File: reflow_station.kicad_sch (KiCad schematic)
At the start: 260 parts, among them IC1 AMC23C10DWVR, IC2 MP100LGN-Z, J1 1731734, J10 DG301-5.0-02P-12-00A_H_, J11 USB_A, J12 USB_C_Receptacle_USB2.0_16P, J13 Conn_ARM_JTAG_SWD_10, J2 1707027, J3 1707027, J4 F52Q-1A7H1-11015, J5 1707027, J6 1707027, J7 DG301-5.0-02P-12-00A_H_, J8 DG301-5.0-02P-12-00A_H_, J9 DG301-5.0-02P-12-00A_H_, M1 Fan_CPU_4pin, M2 Fan_CPU_4pin, M3 Fan_CPU_4pin, M4 Fan_CPU_4pin, P1 IEC_60320_C13_Plug, Q1 BTA16-600B, Q2 BTA16-600B, Q3 BTA16-600B, Q4 BTA16-600B, Q5 KSC1815YTA, SW1 SW_DPST_x2, SW2 SW_DIP_x08, SW3 SW_SPST, SW4 SW_SPST, SW5 SW_SPST, SW6 SW_Push, SW7 SW_SPDT, SW8 SW_SPDT, U1 TPS82130, U10 TPS2051BDBVR, U11 RCLAMP0504F.TCT, U12 STM32F469VITx, U13 RCLAMP0504F.TCT, U14 RCLAMP0504F.TCT, U2 RAC20-12SK, U3 MOC3023M, U4 MOC3023M, U5 TPS82130, U6 MOC3023M, U7 MOC3023M, U8 ADS1118IDGS, U9 ADS1118IDGS, Y1 25MHz, Y2 32.768kHz

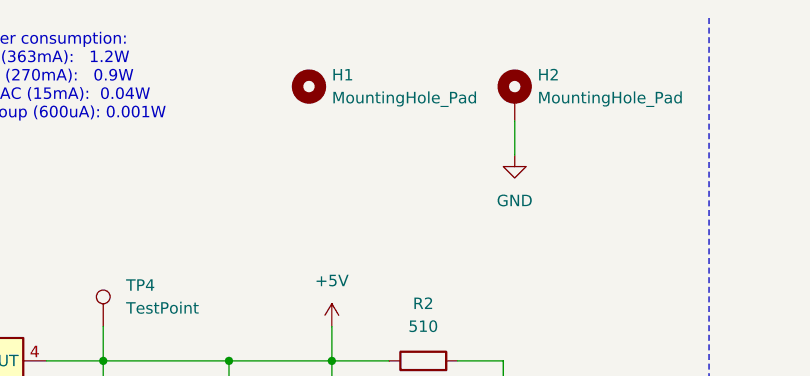
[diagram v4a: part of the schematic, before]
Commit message: feat: update library; change 2P connector for heaters
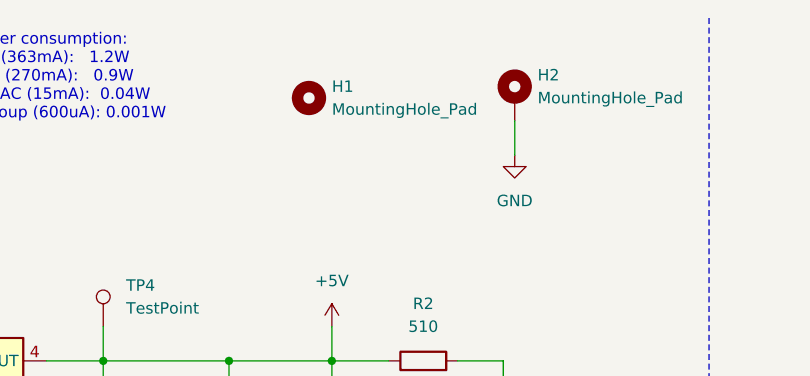
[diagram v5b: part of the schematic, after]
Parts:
- H1: symbol Mechanical:MountingHole -> reflow_station_symbols:MountingHole
- H2, H3, H4: symbol Mechanical:MountingHole_Pad -> reflow_station_symbols:MountingHole_Pad
- J2, J3, J5, J6: footprint reflow_station_library:1707027 -> 1731721; symbol reflow_station_symbols:1707027 -> reflow_station_symbols:1731721; Height 10 -> 18.2; Manufacturer_Part_Number 1707027 -> 1731721
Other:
- moved on the sheet: H1
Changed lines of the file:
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@@
 	)
 	(symbol
-		(lib_id "reflow_station_symbols:1707027")
+		(lib_id "reflow_station_symbols:1731721")
 		(at 1007.11 104.14 90)
 		(mirror x)
@@
 			)
 		)
-		(property "Footprint" "reflow_station_library:1707027"
+		(property "Footprint" "1731721"
 			(at 1102.03 120.65 0)
 			(hide yes)
@@
 			)
 		)
-		(property "Datasheet" "https://www.phoenixcontact.com/en-us/products/printed-circuit-board-terminal-gmkdsn-15-2-762-1707027?type=pdf"
+		(property "Datasheet" "https://www.phoenixcontact.com/en-us/products/printed-circuit-board-terminal-gmkds-3-2-762-1731721?type=pdf"
 			(at 1202.03 120.65 0)
 			(hide yes)
@@
 			)
 		)
-		(property "Description" "GMKDSN 1,5/ 2-7,62 - Printed circuit board terminal, nominal current: 16 A, rated voltage (III/2): 630 V, nominal cross section: 1.5 mm<sup>2</sup>, number of potentials: 2, number of rows: 1, number of positions per row: 2, product range: GMKDSN 1,5, pitch: 7.62 mm, connection method: Screw connection with tension sleeve, screw head form: L Slotted, mounting: Wave soldering, conductor/PCB connection direction: 0 , color: green, Pin layout: Linear pinning, Solder pin [P]: 3.5 mm, number of solder pins per"
+		(property "Description" "GMKDS 3/ 2-7,62 - Printed circuit board terminal, nominal current: 24 A, rated voltage (III/2): 630 V, nominal cross section: 2.5 mm<sup>2</sup>, number of potentials: 2, number of rows: 1, number of positions per row: 2, product range: GMKDS 3, pitch: 7.62 mm, connection method: Screw connection with tension sleeve, screw head form: L Slotted, mounting: Wave soldering, conductor/PCB connection direction: 0 , color: green, Pin layout: Linear pinning, Solder pin [P]: 5 mm, number of solder pins per potentia"
 			(at 1007.11 104.14 0)
 			(hide yes)
@@
 			)
 		)
-		(property "Height" "10"
+		(property "Height" "18.2"
 			(at 1402.03 120.65 0)
 			(hide yes)
@@
 			)
 		)
-		(property "Manufacturer_Part_Number" "1707027"
+		(property "Manufacturer_Part_Number" "1731721"
 			(at 1802.03 120.65 0)
 			(hide yes)
@@
 	)
 	(symbol
-		(lib_id "Mechanical:MountingHole_Pad")
+		(lib_id "reflow_station_symbols:MountingHole_Pad")
 		(at 63.5 515.62 0)
 		(unit 1)
@@
 	)
 	(symbol
-		(lib_id "reflow_station_symbols:1707027")
+		(lib_id "reflow_station_symbols:1731721")
 		(at 1158.24 218.44 90)
 		(mirror x)
@@
 			)
 		)
-		(property "Footprint" "reflow_station_library:1707027"
+		(property "Footprint" "1731721"
 			(at 1253.16 234.95 0)
 			(hide yes)
@@
 			)
 		)
-		(property "Datasheet" "https://www.phoenixcontact.com/en-us/products/printed-circuit-board-terminal-gmkdsn-15-2-762-1707027?type=pdf"
+		(property "Datasheet" "https://www.phoenixcontact.com/en-us/products/printed-circuit-board-terminal-gmkds-3-2-762-1731721?type=pdf"
 			(at 1353.16 234.95 0)
 			(hide yes)
@@
 			)
 		)
-		(property "Description" "GMKDSN 1,5/ 2-7,62 - Printed circuit board terminal, nominal current: 16 A, rated voltage (III/2): 630 V, nominal cross section: 1.5 mm<sup>2</sup>, number of potentials: 2, number of rows: 1, number of positions per row: 2, product range: GMKDSN 1,5, pitch: 7.62 mm, connection method: Screw connection with tension sleeve, screw head form: L Slotted, mounting: Wave soldering, conductor/PCB connection direction: 0 , color: green, Pin layout: Linear pinning, Solder pin [P]: 3.5 mm, number of solder pins per"
+		(property "Description" "GMKDS 3/ 2-7,62 - Printed circuit board terminal, nominal current: 24 A, rated voltage (III/2): 630 V, nominal cross section: 2.5 mm<sup>2</sup>, number of potentials: 2, number of rows: 1, number of positions per row: 2, product range: GMKDS 3, pitch: 7.62 mm, connection method: Screw connection with tension sleeve, screw head form: L Slotted, mounting: Wave soldering, conductor/PCB connection direction: 0 , color: green, Pin layout: Linear pinning, Solder pin [P]: 5 mm, number of solder pins per potentia"
 			(at 1158.24 218.44 0)
 			(hide yes)
@@
 			)
 		)
-		(property "Height" "10"
+		(property "Height" "18.2"
 			(at 1553.16 234.95 0)
 			(hide yes)
@@
 			)
 		)
-		(property "Manufacturer_Part_Number" "1707027"
+		(property "Manufacturer_Part_Number" "1731721"
 			(at 1953.16 234.95 0)
 			(hide yes)
@@
 	)
 	(symbol
-		(lib_id "Mechanical:MountingHole")
-		(at 316.23 20.32 0)
+		(lib_id "reflow_station_symbols:MountingHole")
+		(at 316.23 21.59 0)
 		(unit 1)
 		(body_style 1)
@@
 		(fields_autoplaced yes)
 		(property "Reference" "H1"
-			(at 318.77 19.0499 0)
+			(at 318.77 20.3199 0)
 			(show_name no)
 			(do_not_autoplace no)
@@
 		)
 		(property "Value" "MountingHole_Pad"
-			(at 318.77 21.5899 0)
+			(at 318.77 22.8599 0)
 			(show_name no)
 			(do_not_autoplace no)
@@
 		)
 		(property "Footprint" "MountingHole:MountingHole_3mm"
-			(at 316.23 20.32 0)
+			(at 316.23 21.59 0)
 			(hide yes)
 			(show_name no)
@@
 		)
 		(property "Datasheet" ""
-			(at 316.23 20.32 0)
+			(at 316.23 21.59 0)
 			(hide yes)
 			(show_name no)
@@
 		)
 		(property "Description" "Mounting Hole without connection"
-			(at 316.23 20.32 0)
+			(at 316.23 21.59 0)
 			(hide yes)
 			(show_name no)
@@
 	)
 	(symbol
-		(lib_id "reflow_station_symbols:1707027")
+		(lib_id "reflow_station_symbols:1731721")
 		(at 1007.11 218.44 90)
 		(mirror x)
@@
 			)
 		)
-		(property "Footprint" "reflow_station_library:1707027"
+		(property "Footprint" "1731721"
 			(at 1102.03 234.95 0)
 			(hide yes)
@@
 			)
 		)
-		(property "Datasheet" "https://www.phoenixcontact.com/en-us/products/printed-circuit-board-terminal-gmkdsn-15-2-762-1707027?type=pdf"
+		(property "Datasheet" "https://www.phoenixcontact.com/en-us/products/printed-circuit-board-terminal-gmkds-3-2-762-1731721?type=pdf"
 			(at 1202.03 234.95 0)
 			(hide yes)
@@
 			)
 		)
-		(property "Description" "GMKDSN 1,5/ 2-7,62 - Printed circuit board terminal, nominal current: 16 A, rated voltage (III/2): 630 V, nominal cross section: 1.5 mm<sup>2</sup>, number of potentials: 2, number of rows: 1, number of positions per row: 2, product range: GMKDSN 1,5, pitch: 7.62 mm, connection method: Screw connection with tension sleeve, screw head form: L Slotted, mounting: Wave soldering, conductor/PCB connection direction: 0 , color: green, Pin layout: Linear pinning, Solder pin [P]: 3.5 mm, number of solder pins per"
+		(property "Description" "GMKDS 3/ 2-7,62 - Printed circuit board terminal, nominal current: 24 A, rated voltage (III/2): 630 V, nominal cross section: 2.5 mm<sup>2</sup>, number of potentials: 2, number of rows: 1, number of positions per row: 2, product range: GMKDS 3, pitch: 7.62 mm, connection method: Screw connection with tension sleeve, screw head form: L Slotted, mounting: Wave soldering, conductor/PCB connection direction: 0 , color: green, Pin layout: Linear pinning, Solder pin [P]: 5 mm, number of solder pins per potentia"
 			(at 1007.11 218.44 0)
 			(hide yes)
@@
 			)
 		)
-		(property "Height" "10"
+		(property "Height" "18.2"
 			(at 1402.03 234.95 0)
 			(hide yes)
@@
 			)
 		)
-		(property "Manufacturer_Part_Number" "1707027"
+		(property "Manufacturer_Part_Number" "1731721"
 			(at 1802.03 234.95 0)
 			(hide yes)
@@
 	)
 	(symbol
-		(lib_id "Mechanical:MountingHole_Pad")
+		(lib_id "reflow_station_symbols:MountingHole_Pad")
 		(at 339.09 21.59 0)
 		(unit 1)
@@
 	)
 	(symbol
-		(lib_id "Mechanical:MountingHole_Pad")
+		(lib_id "reflow_station_symbols:MountingHole_Pad")
 		(at 38.1 515.62 0)
 		(unit 1)
@@
 	)
 	(symbol
-		(lib_id "reflow_station_symbols:1707027")
+		(lib_id "reflow_station_symbols:1731721")
 		(at 1158.24 104.14 90)
 		(mirror x)
@@
 			)
 		)
-		(property "Footprint" "reflow_station_library:1707027"
+		(property "Footprint" "1731721"
 			(at 1253.16 120.65 0)
 			(hide yes)
@@
 			)
 		)
-		(property "Datasheet" "https://www.phoenixcontact.com/en-us/products/printed-circuit-board-terminal-gmkdsn-15-2-762-1707027?type=pdf"
+		(property "Datasheet" "https://www.phoenixcontact.com/en-us/products/printed-circuit-board-terminal-gmkds-3-2-762-1731721?type=pdf"
 			(at 1353.16 120.65 0)
 			(hide yes)
@@
 			)
 		)
-		(property "Description" "GMKDSN 1,5/ 2-7,62 - Printed circuit board terminal, nominal current: 16 A, rated voltage (III/2): 630 V, nominal cross section: 1.5 mm<sup>2</sup>, number of potentials: 2, number of rows: 1, number of positions per row: 2, product range: GMKDSN 1,5, pitch: 7.62 mm, connection method: Screw connection with tension sleeve, screw head form: L Slotted, mounting: Wave soldering, conductor/PCB connection direction: 0 , color: green, Pin layout: Linear pinning, Solder pin [P]: 3.5 mm, number of solder pins per"
+		(property "Description" "GMKDS 3/ 2-7,62 - Printed circuit board terminal, nominal current: 24 A, rated voltage (III/2): 630 V, nominal cross section: 2.5 mm<sup>2</sup>, number of potentials: 2, number of rows: 1, number of positions per row: 2, product range: GMKDS 3, pitch: 7.62 mm, connection method: Screw connection with tension sleeve, screw head form: L Slotted, mounting: Wave soldering, conductor/PCB connection direction: 0 , color: green, Pin layout: Linear pinning, Solder pin [P]: 5 mm, number of solder pins per potentia"
 			(at 1158.24 104.14 0)
 			(hide yes)
@@
 			)
 		)
-		(property "Height" "10"
+		(property "Height" "18.2"
 			(at 1553.16 120.65 0)
 			(hide yes)
@@
 			)
 		)
-		(property "Manufacturer_Part_Number" "1707027"
+		(property "Manufacturer_Part_Number" "1731721"
 			(at 1953.16 120.65 0)
 			(hide yes)

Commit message: feat: add proper triac footprint with creepage drill
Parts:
- removed HS1: Heatsink, symbol reflow_station_symbols:Heatsink
- removed U3: MOC3023M, reflow_station_library:DIP-6_W7.62mm_LongPads, symbol reflow_station_symbols:MOC3023M
- added U3: MOC3052M, reflow_station_library:SMDIP-6_W9.53mm, symbol reflow_station_symbols:MOC3052M
- D4: footprint reflow_station_library:MBS_L4.7-W3.8-P2.40-LS7.0-TL -> reflow_station_library:SOP240P700X300-4N; KiLib_Generator (none) -> package/gullwing
- H1: footprint MountingHole:MountingHole_3mm -> reflow_station_library:MountingHole_3mm; now not fitted
- H2, H3, H4: footprint MountingHole:MountingHole_3mm_Pad_Via -> reflow_station_library:MountingHole_3mm_Pad_Via; now not fitted
- J2, J3, J5, J6: footprint 1731721 -> reflow_station_library:1731721
- M1, M2, M3, M4: footprint Connector_JST:JST_PH_B4B-PH-K_1x04_P2.00mm_Vertical -> reflow_station_library:JST_PH_B4B-PH-K_1x04_P2.00mm_Vertical
- Q1, Q2, Q3, Q4: footprint reflow_station_library:TO-220-3_Vertical -> reflow_station_library:TO-220-3_Vertical_Staggered; Creación (none) -> 2026-09-16; Descripción 2 (none) -> Snnn - Data or Component Name; KiLib_Generator package/TO_SOT/THT -> (none); Texto 1 (none) -> T1; Texto 2 (none) -> T2
- R11, R12, R33, R34: value 330 1W fusible -> 470 1W fusible
- SW3, SW4, SW5: footprint Connector_JST:JST_PH_B2B-PH-K_1x02_P2.00mm_Vertical -> reflow_station_library:JST_PH_B2B-PH-K_1x02_P2.00mm_Vertical
- U4, U6, U7: value MOC3023M -> MOC3052M; footprint reflow_station_library:DIP-6_W7.62mm_LongPads -> reflow_station_library:SMDIP-6_W9.53mm; symbol reflow_station_symbols:MOC3023M -> reflow_station_symbols:MOC3052M
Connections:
- net HEATER_A#: now also U3.2
- net L: no longer Q1.2 (A2), Q2.2 (A2), Q3.2 (A2), Q4.2 (A2), R11.2, R12.2, R18.1, R19.1, R33.2, R34.2, R35.1, R36.1, RV1.1, RV2.1, RV3.1, RV4.1
- net L_FUSED: now also Q1.2 (A2), Q2.2 (A2), Q3.2 (A2), Q4.2 (A2), R11.2, R12.2, R18.1, R19.1, R33.2, R34.2, R35.1, R36.1, RV1.1, RV2.1, RV3.1, RV4.1
- net at Q1.3 (G): now also U3.4
- net at R24.2: now also U3.1
- net at R11.1: now also U3.6

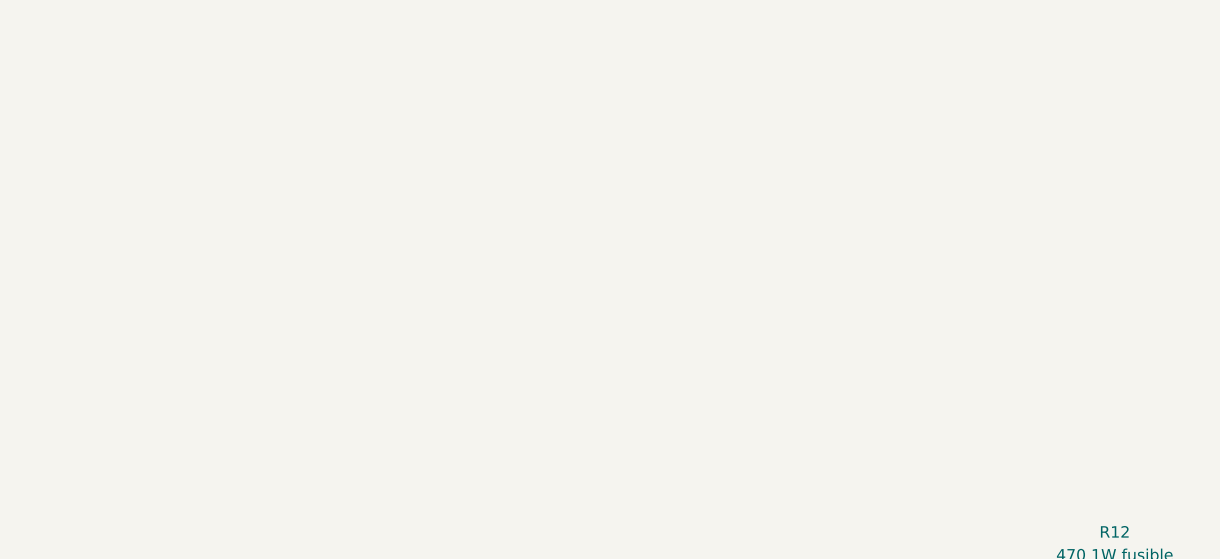
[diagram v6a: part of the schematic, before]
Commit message: feat: route high voltage traces
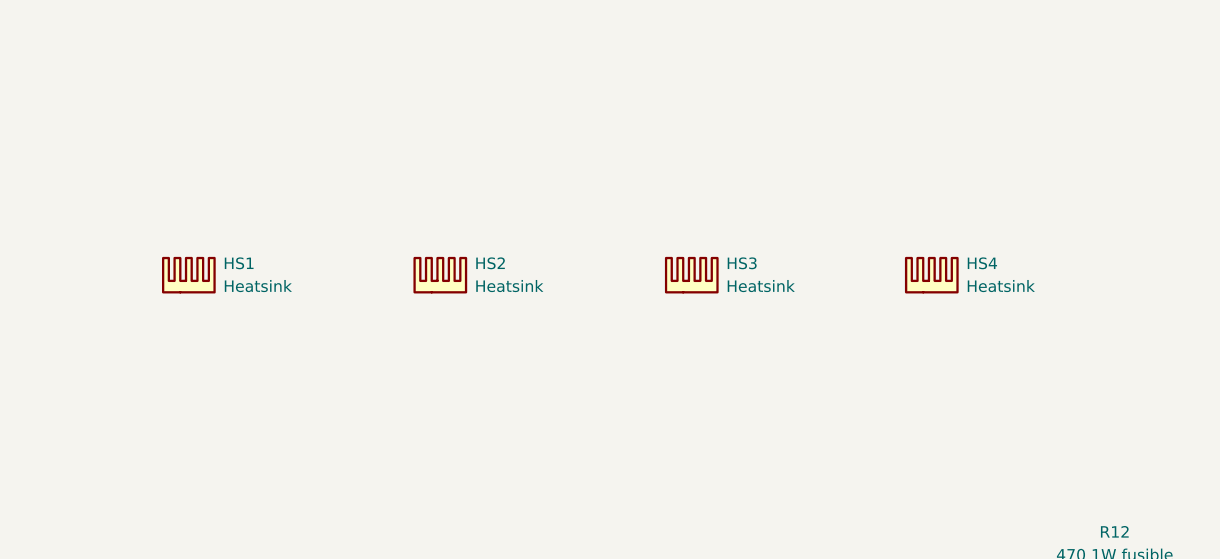
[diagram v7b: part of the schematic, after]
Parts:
- added HS1, HS2, HS3, HS4: Heatsink, Heatsink:Heatsink_Stonecold_HS-132_32x14mm_2xFixation1.5mm, symbol Mechanical:Heatsink
- R18, R19, R35, R36: footprint reflow_station_library:R_0805_2012Metric_Pad1.20x1.40mm_HandSolder -> Capacitor_SMD:C_1210_3225Metric

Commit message: feat: write down whole BOM
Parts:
- C1: Mfr.No (none) -> R474N31005001K; Supplier (none) -> TME; Supplier_Link (none) -> https://www.tme.eu/pl/details/r474n31005001k/kondensatory-f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
- C10, C20, C23, C24, C27, C28, C29, C30, C31, C33, C37, C38, C40, C41, C42, C43, C44, C45, C46, C47, C48, C49, C51, C53, C55, C56, C6: JLCPCB_PartNo (none) -> C307331; Mfr.No (none) -> CL05B104KB54PNC; Package (none) -> 0402; Supplier (none) -> JLCPCB; Supplier_Link (none) -> https://jlcpcb.com/partdetail/291005-CL05B104KB54PNC/C307331
- C11: JLCPCB_PartNo (none) -> C1604; Mfr.No (none) -> 0603B222K500NT; Package (none) -> 0603; Supplier (none) -> JLCPCB; Supplier_Link (none) -> https://jlcpcb.com/partdetail/1956-0603B222K500NT/C1604
- C12, C13, C21, C22: Mfr.No (none) -> B32921C3103M189; Supplier (none) -> TME; Supplier_Link (none) -> https://www.tme.eu/pl/details/b32921c3103m189/kondensatory-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
- C14, C4: JLCPCB_PartNo (none) -> C13585; Mfr.No (none) -> CL31A106KBHNNNE; Package (none) -> 1206; Supplier (none) -> JLCPCB; Supplier_Link (none) -> https://jlcpcb.com/partdetail/14236-CL31A106KBHNNNE/C13585
- C15: JLCPCB_PartNo (none) -> C12891; Mfr.No (none) -> CL31A226KAHNNNE; Package (none) -> 1206; Supplier (none) -> JLCPCB; Supplier_Link (none) -> https://jlcpcb.com/partdetail/13537-CL31A226KAHNNNE/C12891
- C16: JLCPCB_PartNo (none) -> C1620; Mfr.No (none) -> 0603B471K500NT; Package (none) -> 0603; Supplier (none) -> JLCPCB; Supplier_Link (none) -> https://jlcpcb.com/partdetail/1972-0603B471K500NT/C1620
- C17: JLCPCB_PartNo (none) -> C46527540; Mfr.No (none) -> RVT1V221M0810ZY; Package (none) -> D8xL10.5mm; Supplier (none) -> JLCPCB; Supplier_Link (none) -> https://jlcpcb.com/partdetail/ChengTao-RVT1V221M0810ZY/C465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
- C18, C8: JLCPCB_PartNo (none) -> C2193561; Mfr.No (none) -> GCM1555C1H431JA16D; Package (none) -> 0402; Supplier (none) -> JLCPCB; Supplier_Link (none) -> https://jlcpcb.com/partdetail/2285629-GCM1555C1H431JA16D/C2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
- C19, C39: JLCPCB_PartNo (none) -> C1779; Mfr.No (none) -> CL21A475KAQNNNE; Package (none) -> 0805; Supplier (none) -> JLCPCB; Supplier_Link (none) -> https://jlcpcb.com/partdetail/2131-CL21A475KAQNNNE/C1779
- C2: value 100n 25V -> 100n; footprint reflow_station_library:C_0603_1608Metric_Pad1.08x0.95mm_HandSolder -> reflow_station_library:C_0402_1005Metric; JLCPCB_PartNo (none) -> C307331; Mfr.No (none) -> CL05B104KB54PNC; Package (none) -> 0402; Supplier (none) -> JLCPCB; Supplier_Link (none) -> https://jlcpcb.com/partdetail/291005-CL05B104KB54PNC/C307331
- C25, C26, C35, C36, C54, C57, C7, C9: JLCPCB_PartNo (none) -> C28323; Mfr.No (none) -> CL21B105KBFNNNE; Package (none) -> 0805; Supplier (none) -> JLCPCB; Supplier_Link (none) -> https://jlcpcb.com/partdetail/29074-CL21B105KBFNNNE/C28323
- C3: value 47u 25V -> 47u; Mfr.No (none) -> C2220C476M3R2CAUTO; Package (none) -> 2220; Supplier (none) -> TME; Supplier_Link (none) -> https://www.tme.eu/pl/en/details/c2220c476m3r2cauto/mlcc-sm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
- C32, C34: JLCPCB_PartNo (none) -> C15195; Mfr.No (none) -> CL05B103KB5NNNC; Package (none) -> 0402; Supplier (none) -> JLCPCB; Supplier_Link (none) -> https://jlcpcb.com/partdetail/15869-CL05B103KB5NNNC/C15195
- C5, C50: JLCPCB_PartNo (none) -> C96123; Mfr.No (none) -> CL31A476MPHNNNE; Package (none) -> 1206; Supplier (none) -> JLCPCB; Supplier_Link (none) -> https://jlcpcb.com/partdetail/97327-CL31A476MPHNNNE/C96123
- C52, C60, C61: JLCPCB_PartNo (none) -> C23630; Mfr.No (none) -> CL10A225KO8NNNC; Package (none) -> 0603; Supplier (none) -> JLCPCB; Supplier_Link (none) -> https://jlcpcb.com/partdetail/24366-CL10A225KO8NNNC/C23630
- C58, C59: JLCPCB_PartNo (none) -> C32949; Mfr.No (none) -> CL05C100JB5NNNC; Package (none) -> 0402; Supplier (none) -> JLCPCB; Supplier_Link (none) -> https://jlcpcb.com/partdetail/33914-CL05C100JB5NNNC/C32949
- C62, C63: JLCPCB_PartNo (none) -> C1552; Mfr.No (none) -> 0402CG1R5C500NT; Package (none) -> 0402; Supplier (none) -> JLCPCB; Supplier_Link (none) -> https://jlcpcb.com/partdetail/1904-0402CG1R5C500NT/C1552
- D1, D10, D2, D5, D7, D8: JLCPCB_PartNo (none) -> C2286; Mfr.No (none) -> KT-0603R; Package (none) -> 0603; Supplier (none) -> JLCPCB; Supplier_Link (none) -> https://jlcpcb.com/partdetail/Hubei_KENTOElec-KT0603R/C2286
- D11: JLCPCB_PartNo (none) -> C34499; Mfr.No (none) -> KT-0805W; Package (none) -> 0805; Supplier (none) -> JLCPCB; Supplier_Link (none) -> https://jlcpcb.com/partdetail/Hubei_KENTOElec-KT0805W/C34499
- D3: JLCPCB_PartNo (none) -> C19726; Mfr.No (none) -> BAT54SLT1G; Package (none) -> SOT-23; Supplier (none) -> JLCPCB; Supplier_Link (none) -> https://jlcpcb.com/partdetail/onsemi-BAT54SLT1G/C19726
- D4: JLCPCB_PartNo (none) -> C2488; Mfr.No (none) -> MB10S-50MIL; Package (none) -> MBS; Supplier (none) -> JLCPCB; Supplier_Link (none) -> https://jlcpcb.com/partdetail/2865-MB10S50MIL/C2488
- D6: JLCPCB_PartNo (none) -> C2297; Mfr.No (none) -> KT-0805G; Package (none) -> 0805; Supplier (none) -> JLCPCB; Supplier_Link (none) -> https://jlcpcb.com/partdetail/Hubei_KENTOElec-KT0805G/C2297
- D9: JLCPCB_PartNo (none) -> C2296; Mfr.No (none) -> KT-0805Y; Package (none) -> 0805; Supplier (none) -> JLCPCB; Supplier_Link (none) -> https://jlcpcb.com/partdetail/Hubei_KENTOElec-KT0805Y/C2296
- F1: value Fuse 15A -> Fuse 20A
- HS1, HS2, HS3, HS4: footprint Heatsink:Heatsink_Stonecold_HS-132_32x14mm_2xFixation1.5mm -> reflow_station_library:Heatsink_Stonecold_HS-132_32x14mm_2xFixation1.5mm; symbol Mechanical:Heatsink -> reflow_station_symbols:Heatsink; Mfr.No (none) -> SK 75 50 SA-TO 220; Supplier (none) -> TME; Supplier_Link (none) -> https://www.tme.eu/pl/en/details/sk75_50_sa-to220/heatsinks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
- IC1: JLCPCB_PartNo (none) -> C5943166; Manufacturer_Part_Number AMC23C10DWVR -> (none); Mfr.No (none) -> AMC23C10DWVR; Package (none) -> SOIC-8; Supplier (none) -> JLCPCB; Supplier_Link (none) -> https://jlcpcb.com/partdetail/TexasInstruments-AMC23C10DWVR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
- IC2: JLCPCB_PartNo (none) -> C17183900; Manufacturer_Part_Number MP100LGN-Z -> (none); Mfr.No (none) -> MP100LGN-Z; Package (none) -> SOIC-8; Supplier (none) -> JLCPCB; Supplier_Link (none) -> https://jlcpcb.com/partdetail/Monolithic_PowerSystems-MP100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
- J1: Manufacturer_Part_Number 1731734 -> (none); Mfr.No (none) -> 1731734; Supplier (none) -> TME; Supplier_Link (none) -> https://www.tme.eu/pl/details/gmkds3_3-7.62/listwy-zaciskow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
- J10, J7, J8, J9: Manufacturer_Part_Number DG301-5.0-02P-12-00A(H) -> (none); Mfr.No (none) -> DG301-5.0-02P-12-00A(H); Supplier (none) -> TME; Supplier_Link (none) -> https://www.tme.eu/pl/en/details/dg301-5.0-2p12/pcb-termina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
- J11: Supplier (none) -> TME; Supplier_Link (none) -> https://www.tme.eu/pl/en/details/mx-67643-0910/usb-ieee1394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
- J12: JLCPCB_PartNo (none) -> C2927038; Mfr.No (none) -> USB-TYPE-C-018; Supplier (none) -> JLCPCB; Supplier_Link (none) -> https://jlcpcb.com/partdetail/DEALON-USB_TYPE_C018/C2927038
- J13: JLCPCB_PartNo (none) -> C42372547; Mfr.No (none) -> HX JN1.27-2x5P ZZ H4.9; Supplier (none) -> JLCPCB; Supplier_Link (none) -> https://jlcpcb.com/partdetail/hanxia-HX_JN1_27_2x5P_ZZ_H49/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
- J2, J3, J5, J6: Manufacturer_Part_Number 1731721 -> (none); Mfr.No (none) -> 1731721; Supplier (none) -> TME; Supplier_Link (none) -> https://www.tme.eu/pl/details/gmkds3_2-7.62/listwy-zaciskow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
- J4: Manufacturer_Part_Number F52Q-1A7H1-11015 -> (none); Mfr.No (none) -> F52Q-1A7H1-11015; Supplier (none) -> MOUSER; Supplier_Link (none) -> https://www.mouser.pl/en/ProductDetail/Amphenol-Aorora/F52Q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
- L1: value FCM1608KF-601T03 -> 600R @ 100MHz; Additional_Info (none) -> C19330 is in greater availability; JLCPCB_PartNo (none) -> C141723; Mfr.No (none) -> FCM1608KF-601T03; Replacement_Mfr.No (none) -> BLM18AG601SN1D; Supplier (none) -> JLCPCB; Supplier_Link (none) -> https://jlcpcb.com/partdetail/TAITECH-FCM1608KF601T03/C1417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
- L2, L3, L4: JLCPCB_PartNo (none) -> C88984; Mfr.No (none) -> BLM18PG330SN1D; Supplier (none) -> JLCPCB; Supplier_Link (none) -> https://jlcpcb.com/partdetail/MurataElectronics-BLM18PG330S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
- LS1: Manufacturer_Part_Number PS1240P02BT -> (none); Mfr.No (none) -> PS1240P02BT; Supplier (none) -> MOUSER; Supplier_Link (none) -> https://www.mouser.pl/en/ProductDetail/TDK/PS1240P02BT?qs=d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
- M1, M2, M3, M4: Mfr.No (none) -> B4B-PH-K-S (LF)(SN); Supplier (none) -> TME; Supplier_Link (none) -> https://www.tme.eu/pl/details/b4b-ph-k-s/zlacza-sygnalowe-r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
- P1: value IEC_60320_C13_Plug -> C20 Plug 20A
- Q1, Q2, Q3, Q4: Additional_Info (none) -> T1635H-6I has Igt=35mA but has max Tj at 150 'C; Creación 2026-09-16 -> (none); Descripción 2 Snnn - Data or Component Name -> (none); Mfr.No (none) -> BTA16-600BRG; Package (none) -> TO-220; Replacement_Mfr.No (none) -> BTA08-600BRG; T1635H-6I; Supplier (none) -> TME; Supplier_Link (none) -> https://www.tme.eu/pl/en/details/bta16-600brg/triacs/stmicr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
- Q5: footprint reflow_station_library:PinHeader_1x03_P1.00mm_Vertical -> reflow_station_library:TO-92L_Inline_Wide; Mfr.No (none) -> KSC1815YTA; Package (none) -> TO92; Supplier (none) -> TME; Supplier_Link (none) -> https://www.tme.eu/pl/en/details/ksc1815yta/npn-tht-transis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
- R1, R42: JLCPCB_PartNo (none) -> C11702; Mfr.No (none) -> 0402WGF1001TCE; Package (none) -> 0402; Supplier (none) -> JLCPCB; Supplier_Link (none) -> https://jlcpcb.com/partdetail/12256-0402WGF1001TCE/C11702
- R10, R14, R15, R16, R17, R4, R5, R75, R9: JLCPCB_PartNo (none) -> C17168; Mfr.No (none) -> 0402WGF0000TCE; Package (none) -> 0402; Supplier (none) -> JLCPCB; Supplier_Link (none) -> https://jlcpcb.com/partdetail/17853-0402WGF0000TCE/C17168
- R11, R12, R33, R34: footprint reflow_station_library:R_Axial_DIN0207_L6.3mm_D2.5mm_P10.16mm_Horizontal -> reflow_station_library:R_Axial_DIN0411_L9.9mm_D3.6mm_P15.24mm_Horizontal; Mfr.No (none) -> FRN01WK0471A10; Supplier (none) -> TME; Supplier_Link (none) -> https://www.tme.eu/pl/details/nfr1w-470r/rezystory-tht/roya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
- R13: JLCPCB_PartNo (none) -> C22859; Mfr.No (none) -> 0603WAF100JT5E; Package (none) -> 0603; Supplier (none) -> JLCPCB; Supplier_Link (none) -> https://jlcpcb.com/partdetail/23586-0603WAF100JT5E/C22859
- R18, R19, R35, R36: footprint Capacitor_SMD:C_1210_3225Metric -> reflow_station_library:C_1210_3225Metric; JLCPCB_PartNo (none) -> C407192; Mfr.No (none) -> 1210W2F330JT5E; Package (none) -> 1210; Supplier (none) -> JLCPCB; Supplier_Link (none) -> https://jlcpcb.com/partdetail/395749-1210W2F330JT5E/C407192
- R2: JLCPCB_PartNo (none) -> C25123; Mfr.No (none) -> 0402WGF5100TCE; Package (none) -> 0402; Supplier (none) -> JLCPCB; Supplier_Link (none) -> https://jlcpcb.com/partdetail/25866-0402WGF5100TCE/C25123
- R20, R21, R22: value 1.09M 1% -> 1.09M; Mfr.No (none) -> TNPW12061M09BEEN; Package (none) -> 1206; Supplier (none) -> MOUSER; Supplier_Link (none) -> https://www.mouser.pl/en/ProductDetail/Vishay/TNPW12061M09B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
- R23: JLCPCB_PartNo (none) -> C17902; Mfr.No (none) -> 1206W4F1002T5E; Package (none) -> 1206; Supplier (none) -> JLCPCB; Supplier_Link (none) -> https://jlcpcb.com/partdetail/18590-1206W4F1002T5E/C17902
- R24, R25, R37, R38: JLCPCB_PartNo (none) -> C25130; Mfr.No (none) -> 0402WGF6800TCE; Package (none) -> 0402; Supplier (none) -> JLCPCB; Supplier_Link (none) -> https://jlcpcb.com/partdetail/25873-0402WGF6800TCE/C25130
- R26, R31, R32, R7, R8: JLCPCB_PartNo (none) -> C25741; Mfr.No (none) -> 0402WGF1003TCE; Package (none) -> 0402; Supplier (none) -> JLCPCB; Supplier_Link (none) -> https://jlcpcb.com/partdetail/26484-0402WGF1003TCE/C25741
- R27, R47, R48, R49, R50, R51, R52: JLCPCB_PartNo (none) -> C25104; Mfr.No (none) -> 0402WGF3300TCE; Package (none) -> 0402; Supplier (none) -> JLCPCB; Supplier_Link (none) -> https://jlcpcb.com/partdetail/25847-0402WGF3300TCE/C25104
- R28: JLCPCB_PartNo (none) -> C122546; Mfr.No (none) -> 0402WGF3093TCE; Package (none) -> 0402; Supplier (none) -> JLCPCB; Supplier_Link (none) -> https://jlcpcb.com/partdetail/123815-0402WGF3093TCE/C122546
- R29: value 90.9k 1% -> 90.9k; JLCPCB_PartNo (none) -> C26989; Mfr.No (none) -> 0402WGF9092TCE; Package (none) -> 0402; Supplier (none) -> JLCPCB; Supplier_Link (none) -> https://jlcpcb.com/partdetail/27738-0402WGF9092TCE/C26989
- R3: JLCPCB_PartNo (none) -> C27011; Mfr.No (none) -> 0402WGF5233TCE; Package (none) -> 0402; Supplier (none) -> JLCPCB; Supplier_Link (none) -> https://jlcpcb.com/partdetail/27760-0402WGF5233TCE/C27011
- R30: value 10.2k 1% -> 10.2k; JLCPCB_PartNo (none) -> C11660; Mfr.No (none) -> 0402WGF1022TCE; Package (none) -> 0402; Supplier (none) -> JLCPCB; Supplier_Link (none) -> https://jlcpcb.com/partdetail/12214-0402WGF1022TCE/C11660
- R39, R40, R41, R43, R44, R45, R46, R54, R55, R56, R57, R74, R76, R77, R78: JLCPCB_PartNo (none) -> C25744; Mfr.No (none) -> 0402WGF1002TCE; Package (none) -> 0402; Supplier (none) -> JLCPCB; Supplier_Link (none) -> https://jlcpcb.com/partdetail/26487-0402WGF1002TCE/C25744
- R53: JLCPCB_PartNo (none) -> C25563; Mfr.No (none) -> 0402WGJ0473TCE; Package (none) -> 0402; Supplier (none) -> JLCPCB; Supplier_Link (none) -> https://jlcpcb.com/partdetail/26306-0402WGJ0473TCE/C25563
- R58, R59, R64, R65, R66, R67, R72, R73: JLCPCB_PartNo (none) -> C26083; Mfr.No (none) -> 0402WGF1004TCE; Package (none) -> 0402; Supplier (none) -> JLCPCB; Supplier_Link (none) -> https://jlcpcb.com/partdetail/26826-0402WGF1004TCE/C26083
- R6: footprint reflow_station_library:R_Axial_DIN0922_L20.0mm_D9.0mm_P25.40mm_Horizontal -> reflow_station_library:R_Axial_DIN0516_L15.5mm_D5.0mm_P20.32mm_Horizontal; Mfr.No (none) -> PMR03SJ0101A19; Supplier (none) -> TME; Supplier_Link (none) -> https://www.tme.eu/pl/details/pmr3s-100r/rezystory-tht/roya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
- R60, R61, R62, R63, R68, R69, R70, R71: JLCPCB_PartNo (none) -> C6460545; Mfr.No (none) -> RT0402FRE07500RL; Package (none) -> 0402; Supplier (none) -> JLCPCB; Supplier_Link (none) -> https://jlcpcb.com/partdetail/YAGEO-RT0402FRE07500RL/C64605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
- R79, R80: JLCPCB_PartNo (none) -> C25905; Mfr.No (none) -> 0402WGF5101TCE; Package (none) -> 0402; Supplier (none) -> JLCPCB; Supplier_Link (none) -> https://jlcpcb.com/partdetail/26648-0402WGF5101TCE/C25905
- R81: JLCPCB_PartNo (none) -> C25779; Mfr.No (none) -> 0402WGF3302TCE; Package (none) -> 0402; Supplier (none) -> JLCPCB; Supplier_Link (none) -> https://jlcpcb.com/partdetail/26522-0402WGF3302TCE/C25779
- R82: JLCPCB_PartNo (none) -> C23254; Mfr.No (none) -> 0603WAF8202T5E; Package (none) -> 0603; Supplier (none) -> JLCPCB; Supplier_Link (none) -> https://jlcpcb.com/partdetail/23981-0603WAF8202T5E/C23254
- RV1, RV2, RV3, RV4: Mfr.No (none) -> ERZE10A561; Supplier (none) -> TME; Supplier_Link (none) -> https://www.tme.eu/pl/details/erze10a561/warystory-tht/pana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
- SW2: Mfr.No (none) -> DS-08; Supplier (none) -> TME; Supplier_Link (none) -> https://www.tme.eu/pl/details/ds-08/przelaczniki-typu-dip-s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
- SW3, SW4, SW5: Mfr.No (none) -> B2B-PH-K-S (LF)(SN); Supplier (none) -> TME; Supplier_Link (none) -> https://www.tme.eu/pl/details/b2b-ph-k-s/zlacza-sygnalowe-r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
- SW6: Availability Not in stock -> (none); Check_prices https://www.snapeda.com/parts/TS-1088-AR02016/Xunpu/view-pa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 -> (none); Description_1 50mA 4mm 100MΩ 100,000 Times 12V 160gf 3mm 2mm Round Button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 -> (none); JLCPCB_PartNo (none) -> C720477; Mfr.No (none) -> TS-1088-AR02016; Package Package -> (none); SnapEDA_Link https://www.snapeda.com/parts/TS-1088-AR02016/Xunpu/view-pa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 -> (none); Supplier (none) -> JLCPCB; Supplier_Link (none) -> https://jlcpcb.com/partdetail/XUNPU-TS_1088AR02016/C720477
- SW7, SW8: Mfr.No (none) -> ESP1010; Supplier (none) -> TME; Supplier_Link (none) -> https://www.tme.eu/pl/details/esp1010/przelaczniki-suwakowe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
- TP1, TP10, TP11, TP12, TP13, TP14, TP15, TP16, TP17, TP18, TP19, TP2, TP20, TP21, TP22, TP23, TP24, TP25, TP26, TP27, TP28, TP29, TP3, TP30, TP31, TP32, TP33, TP34, TP35, TP36, TP37, TP38, TP39, TP4, TP40, TP5, TP6, TP7, TP8, TP9: now left out of the parts list
- U1, U5: JLCPCB_PartNo (none) -> C473914; Mfr.No (none) -> TPS82130SILR; Package (none) -> USIP-8; Supplier (none) -> JLCPCB; Supplier_Link (none) -> https://jlcpcb.com/partdetail/TexasInstruments-TPS82130SILR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
- U10: JLCPCB_PartNo (none) -> C24593; Mfr.No (none) -> TPS2051BDBVR; Package (none) -> SOT-23-5; Supplier (none) -> JLCPCB; Supplier_Link (none) -> https://jlcpcb.com/partdetail/TexasInstruments-TPS2051BDBVR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
- U11, U13, U14: JLCPCB_PartNo (none) -> C132257; Mfr.No (none) -> RCLAMP0504F.TCT; Package (none) -> SC-70-6L; Supplier (none) -> JLCPCB; Supplier_Link (none) -> https://jlcpcb.com/partdetail/SEMTECH-RCLAMP0504FTCT/C132257
- U12: value STM32F469VITx -> STM32F469VIT6; JLCPCB_PartNo (none) -> C2970187; Mfr.No (none) -> STM32F469VIT6; Package (none) -> LQFP-100(14x14); Supplier (none) -> JLCPCB; Supplier_Link (none) -> https://jlcpcb.com/partdetail/STMicroelectronics-STM32F469V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
- U2: Mfr.No (none) -> RAC20-12SK; Supplier (none) -> TME; Supplier_Link (none) -> https://www.tme.eu/pl/details/rac20-12sk/przetwornice-ac-dc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
- U3, U4, U6, U7: Mfr.No (none) -> MOC3052M; Package (none) -> DIP-6; Supplier (none) -> TME; Supplier_Link (none) -> https://www.tme.eu/pl/details/moc3052m-ons/optotriaki/onsem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
- U8, U9: JLCPCB_PartNo (none) -> C701612; Mfr.No (none) -> ADS1118IDGST; Package (none) -> VSSOP-10-0.5mm; Supplier (none) -> JLCPCB; Supplier_Link (none) -> https://jlcpcb.com/partdetail/TexasInstruments-ADS1118IDGST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
- Y1: JLCPCB_PartNo (none) -> C9006; Mfr.No (none) -> X322525MOB4SI; Package (none) -> SMD3225-4P; Supplier (none) -> JLCPCB; Supplier_Link (none) -> https://jlcpcb.com/partdetail/YXC_CrystalOscillators-X32252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
- Y2: JLCPCB_PartNo (none) -> C528987; Mfr.No (none) -> NX3215SA 32.768KHZ EXS00A-MU00525; Package (none) -> SMD3215-2p; Replacement_Mfr.No (none) -> NX3215SA 32.768KHZ EXS00A-MU00525; Supplier (none) -> JLCPCB; Supplier_Link (none) -> https://jlcpcb.com/partdetail/C528987
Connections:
- net SHIELD is gone; now on net Earth: H3.1, H4.1, J11.SH (Shield), J12.SH (SHIELD), J13.9 (GNDDetect), J4.MP1, J4.MP2, J4.MP3, J4.MP4, L2.2, L3.2, L4.2, U11.2, U13.2, U14.2
